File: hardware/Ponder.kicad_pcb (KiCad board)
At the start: 2 copper layers, 46 x 48.6 mm, 54 parts, among them J1 USB_C_Receptacle_USB2.0, J2 SM03B-SRSS-TB, J3 Conn_ARM_JTAG_SWD_10, SW1 SW_Push, SW2 SW_Push, U1 NCP1117-3.3_SOT223, U2 W25Q128JVS, U3 RP2350_80QFN, X1 ABM8-272-T3

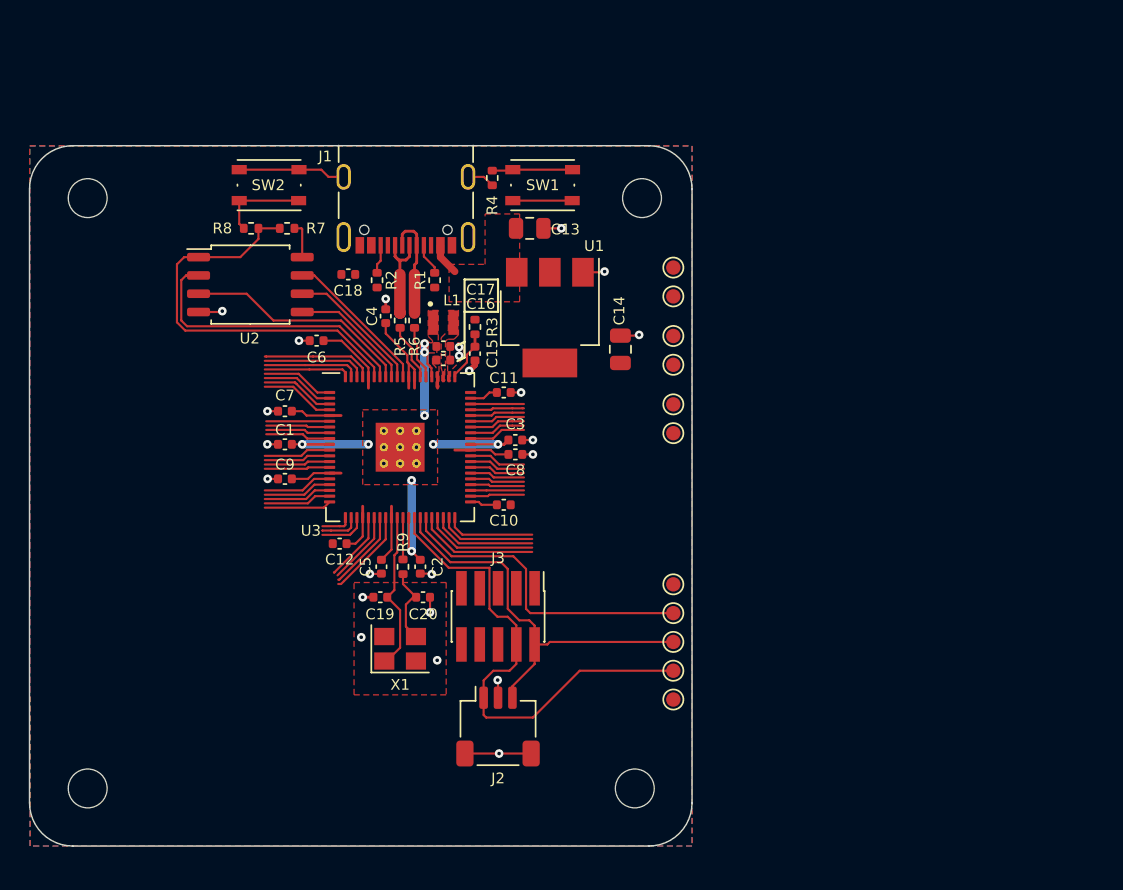
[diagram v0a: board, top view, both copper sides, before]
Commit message: Fixing board outline, aligning USB connector to board edge, clearing some early DRC errors
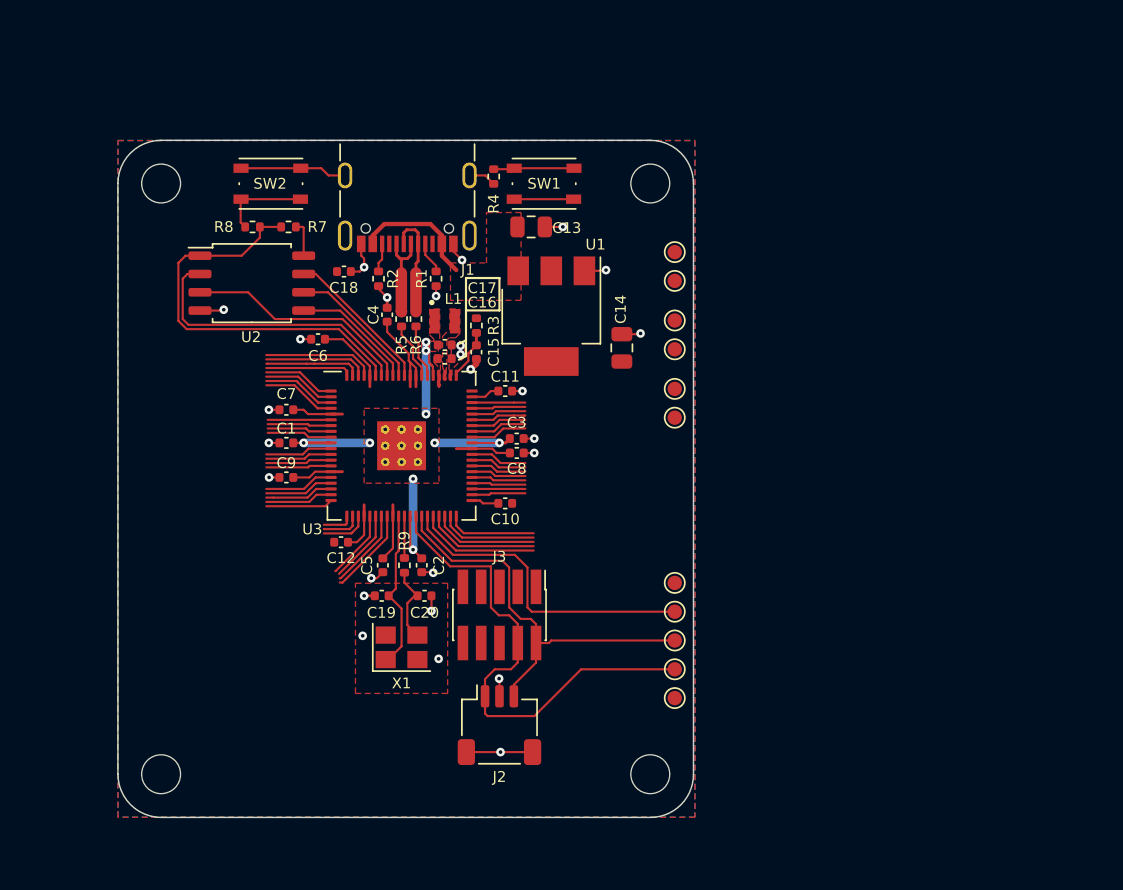
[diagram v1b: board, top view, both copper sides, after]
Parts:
- moved H1 5.20 mm to (123.6, 76.0)
- moved H4 5.19 mm to (123.6, 117.0)
- moved H3 1.46 mm to (157.6, 117.0)
- moved H2 1.17 mm to (157.6, 76.0)
- moved TP1 1.08 mm to (159.3, 82.8)
- moved TP2 1.08 mm to (159.3, 87.5)
- moved TP3 1.08 mm to (159.3, 80.8)
- moved TP4 1.08 mm to (159.3, 85.5)
- moved TP5 1.08 mm to (159.3, 90.2)
- moved TP6 1.08 mm to (159.3, 92.2)
- moved C18 0.36 mm to (136.3, 82.1)
- moved SW2 0.16 mm to (131.2, 76.0)
- moved C4 0.14 mm to (139.3, 85.1)
- moved L1 0.14 mm to (143.3, 85.5)
- moved C1 0.14 mm to (132.3, 94.0)
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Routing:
- net VBUS: track 2.23 -> 8.86 mm
- net GND: track 31.1 -> 37.1 mm, vias 23 -> 26
- net /USB_D-: track 8.05 -> 7.49 mm
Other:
- board size 46 x 48.6 mm -> 40 x 47 mm

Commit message: Adding modstrike box
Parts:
- removed J2: SM03B-SRSS-TB, Connector_JST:JST_SH_SM03B-SRSS-TB_1x03-1MP_P1.00mm_Horizontal
- removed J3: Conn_ARM_JTAG_SWD_10, Connector_PinHeader_1.27mm:PinHeader_2x05_P1.27mm_Vertical_SMD
- added REF**: ModStrike, Ponder:ModStrike, F.Cu at (149.5, 117.5)
- moved TP7 16.7 mm to (144.0, 103.0)
- moved TP9 15.9 mm to (145.0, 104.8)
- moved TP8 14.1 mm to (146.0, 103.0)
- moved TP10 12.3 mm to (147.0, 104.8)
- moved TP11 11.6 mm to (148.0, 103.0)
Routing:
- net /SWCLK: track 34.9 -> 5.02 mm
- net /SWD: track 28.6 -> 6.26 mm
- net /RUN: track 26.2 -> 12.0 mm
- net GND: track 37.1 -> 31.3 mm, vias 26 -> 24
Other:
- board text added: "3V3"
- board text added: "CLK"
- board text added: "GND"
- board text added: "RST"
- board text added: "SWD"

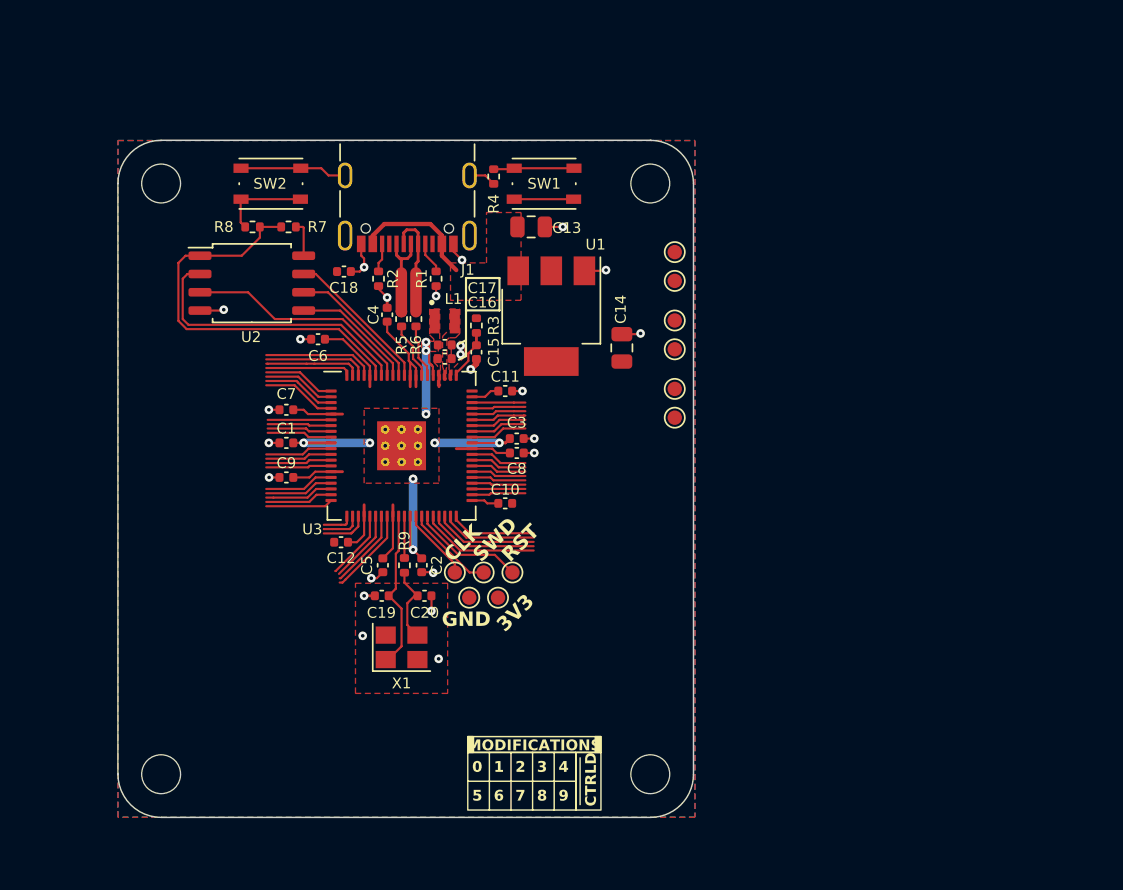
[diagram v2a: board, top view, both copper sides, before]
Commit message: Adding ISOs and 4P headers
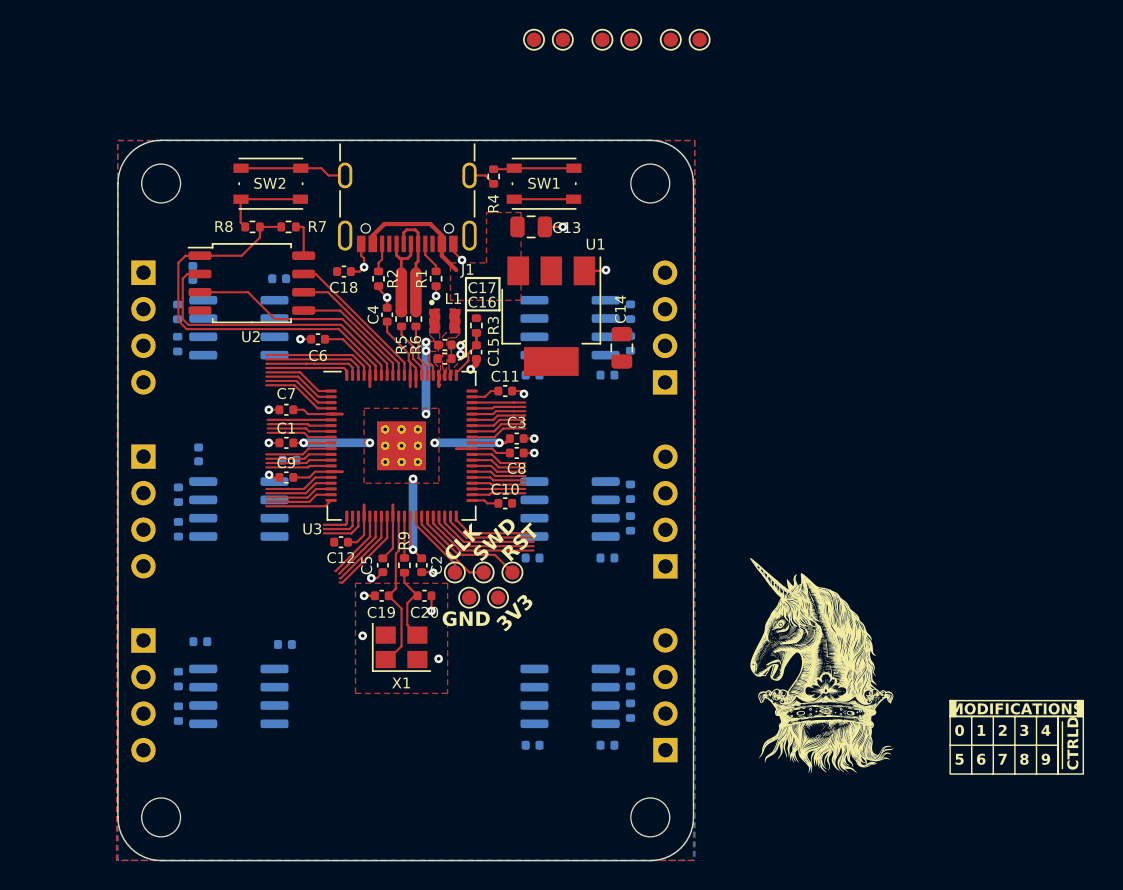
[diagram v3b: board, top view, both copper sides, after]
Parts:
- removed REF**: ModStrike, Ponder:ModStrike
- added C21: 100n, Capacitor_SMD:C_0402_1005Metric, B.Cu at (131.8, 82.6)
- added C22: 100n, Capacitor_SMD:C_0402_1005Metric, B.Cu at (125.8, 82.2)
- added C23: 100n, Capacitor_SMD:C_0402_1005Metric, B.Cu at (132.5, 95.2)
- added C24: 100n, Capacitor_SMD:C_0402_1005Metric, B.Cu at (126.2, 94.8)
- added C25: 100n, Capacitor_SMD:C_0402_1005Metric, B.Cu at (132.2, 108.0)
- added C26: 100n, Capacitor_SMD:C_0402_1005Metric, B.Cu at (149.4, 115.0)
- added C27: 100n, Capacitor_SMD:C_0402_1005Metric, B.Cu at (126.3, 107.8)
- added C28: 100n, Capacitor_SMD:C_0402_1005Metric, B.Cu at (154.6, 115.0)
- added C29: 100n, Capacitor_SMD:C_0402_1005Metric, B.Cu at (149.4, 102.0)
- added C30: 100n, Capacitor_SMD:C_0402_1005Metric, B.Cu at (149.4, 89.3)
- added C31: 100n, Capacitor_SMD:C_0402_1005Metric, B.Cu at (154.6, 102.0)
- added C32: 100n, Capacitor_SMD:C_0402_1005Metric, B.Cu at (154.6, 89.3)
- added G1: ModStrike, Ponder:ModStrike, F.Cu at (183.0, 115.0)
- added G2: Crest, Ponder:Crest-10mm, F.Cu at (169.5, 109.5)
- added J2: 2.54 HDR, Connector_PinHeader_2.54mm:PinHeader_1x04_P2.54mm_Horizontal, B.Cu at (122.4, 82.2)
- added J3: 2.54 HDR, Connector_PinHeader_2.54mm:PinHeader_1x04_P2.54mm_Horizontal, B.Cu at (122.4, 95.0)
- added J4: 2.54 HDR, Connector_PinHeader_2.54mm:PinHeader_1x04_P2.54mm_Horizontal, B.Cu at (122.4, 107.7)
- added J5: 2.54 HDR, Connector_PinHeader_2.54mm:PinHeader_1x04_P2.54mm_Horizontal, B.Cu at (158.6, 115.3)
- added J6: 2.54 HDR, Connector_PinHeader_2.54mm:PinHeader_1x04_P2.54mm_Horizontal, B.Cu at (158.6, 102.6)
- added J7: 2.54 HDR, Connector_PinHeader_2.54mm:PinHeader_1x04_P2.54mm_Horizontal, B.Cu at (158.6, 89.8)
- added R10: 50, Resistor_SMD:R_0402_1005Metric, B.Cu at (124.8, 84.9)
- added R11: 50, Resistor_SMD:R_0402_1005Metric, B.Cu at (124.8, 87.1)
- added R12: 50, Resistor_SMD:R_0402_1005Metric, B.Cu at (124.8, 97.6)
- added R13: 50, Resistor_SMD:R_0402_1005Metric, B.Cu at (124.8, 100.0)
- added R14: 50, Resistor_SMD:R_0402_1005Metric, B.Cu at (124.8, 110.4)
- added R15: 50, Resistor_SMD:R_0402_1005Metric, B.Cu at (124.8, 112.8)
- added R16: 50, Resistor_SMD:R_0402_1005Metric, B.Cu at (156.2, 112.6)
- added R17: 50, Resistor_SMD:R_0402_1005Metric, B.Cu at (156.2, 110.4)
- added R18: 50, Resistor_SMD:R_0402_1005Metric, B.Cu at (156.2, 99.6)
- added R19: 50, Resistor_SMD:R_0402_1005Metric, B.Cu at (156.2, 97.4)
- added R20: 50, Resistor_SMD:R_0402_1005Metric, B.Cu at (156.2, 87.1)
- added R21: 50, Resistor_SMD:R_0402_1005Metric, B.Cu at (156.2, 84.9)
- added U4: 18012115411H, Package_SO:SOIC-8_3.9x4.9mm_P1.27mm, B.Cu at (129.0, 86.0)
- added U5: 18012115411H, Package_SO:SOIC-8_3.9x4.9mm_P1.27mm, B.Cu at (129.0, 98.6)
- added U6: 18012115411H, Package_SO:SOIC-8_3.9x4.9mm_P1.27mm, B.Cu at (129.0, 111.6)
- added U7: 18012115411H, Package_SO:SOIC-8_3.9x4.9mm_P1.27mm, B.Cu at (152.0, 111.6)
- added U8: 18012115411H, Package_SO:SOIC-8_3.9x4.9mm_P1.27mm, B.Cu at (152.0, 98.6)
- added U9: 18012115411H, Package_SO:SOIC-8_3.9x4.9mm_P1.27mm, B.Cu at (152.0, 86.0)
- moved TP6 26.3 mm to (161.0, 66.0), turned to 180 degrees
- moved TP5 24.3 mm to (159.0, 66.0), turned to 180 degrees
- moved TP2 21.7 mm to (156.2, 66.0), turned to 180 degrees
- moved TP4 20.1 mm to (154.2, 66.0), turned to 180 degrees
- moved TP1 18.5 mm to (151.5, 66.0), turned to 180 degrees
- moved TP3 17.7 mm to (149.5, 66.0), turned to 180 degrees
- moved H3 3.00 mm to (157.6, 120.0)
- moved H4 3.00 mm to (123.6, 120.0)
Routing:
- net GND: track 31.3 -> 28.6 mm, vias 24 -> 22
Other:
- board size 40 x 47 mm -> 40 x 50 mm
